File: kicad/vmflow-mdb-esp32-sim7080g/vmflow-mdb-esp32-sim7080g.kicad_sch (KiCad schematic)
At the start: 56 parts, among them J1 MDB_Connector, J2 USB_C_Receptacle_USB2.0_16P, J3 Conn_02x11_Odd_Even, J4 JAE_SIM_Card_SF72S006, J5 Conn_Coaxial, J6 Conn_Coaxial, SW1 SW_Push, U1 TLP785, U2 SIM7080G, U3 ESP32-S3FH4R2, U4 TLP785, U5 LM2594HVM-3.3, Y1 Crystal_GND24

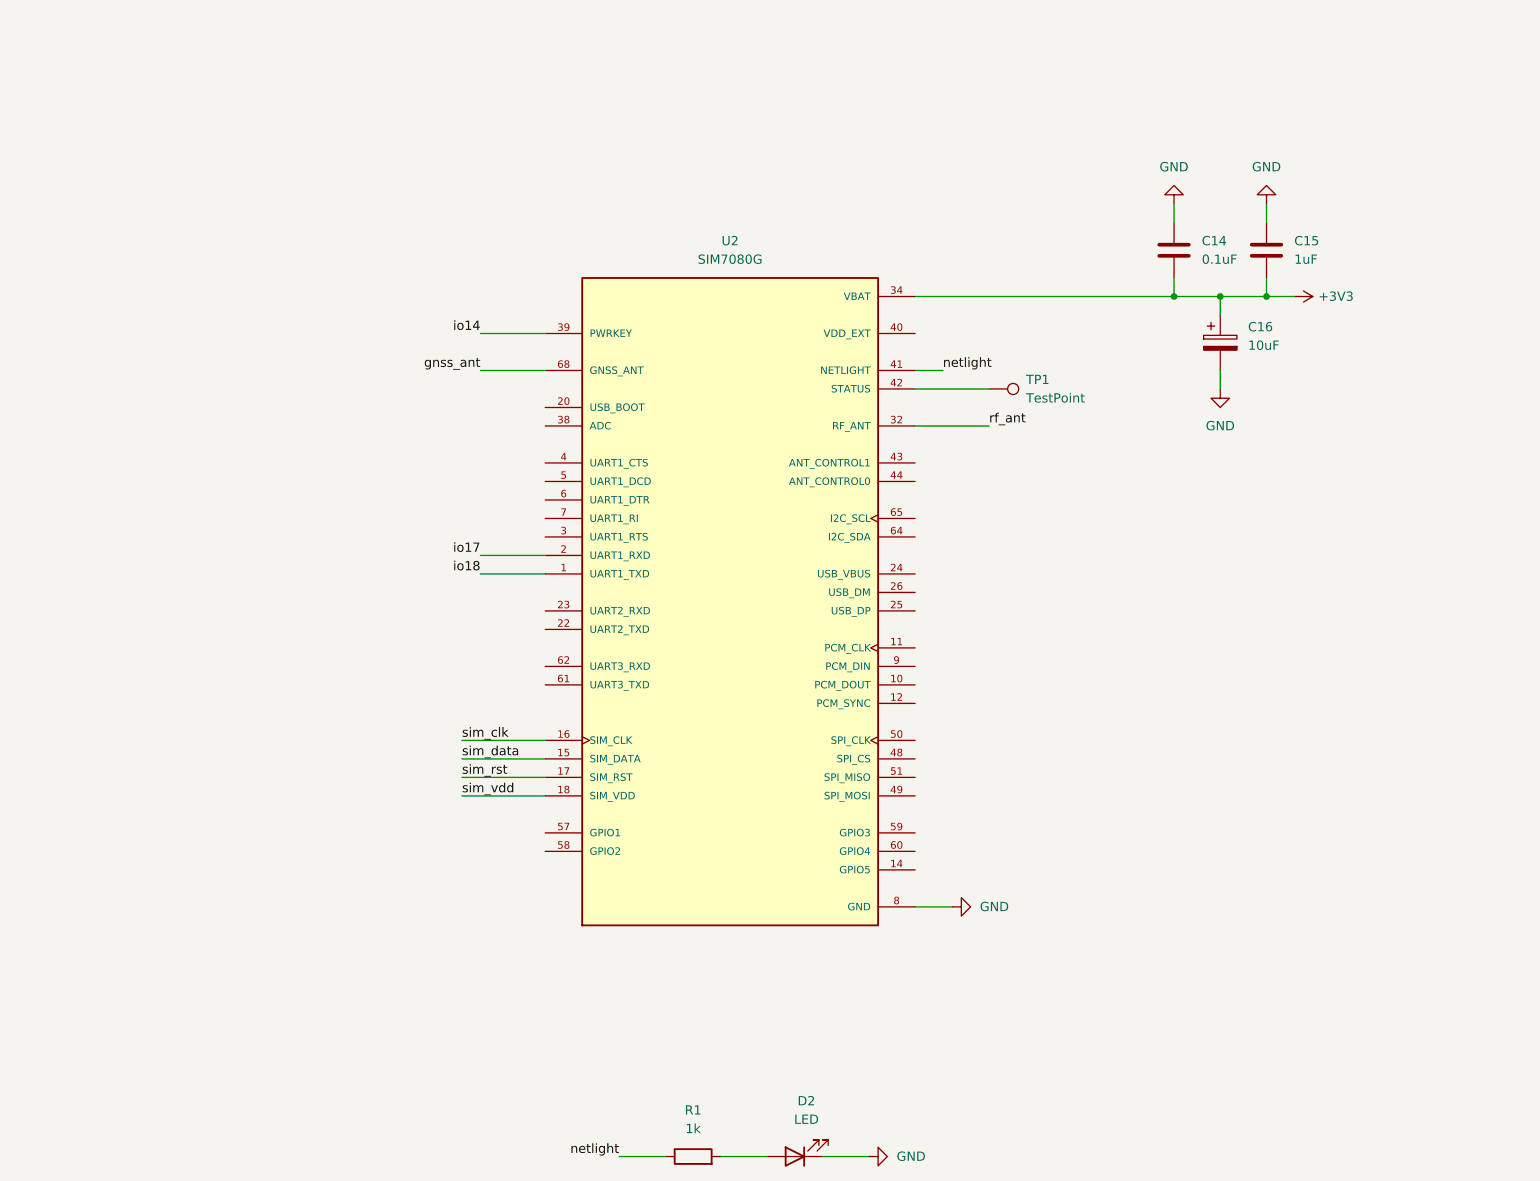
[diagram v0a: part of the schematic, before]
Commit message: Implementing transistor control
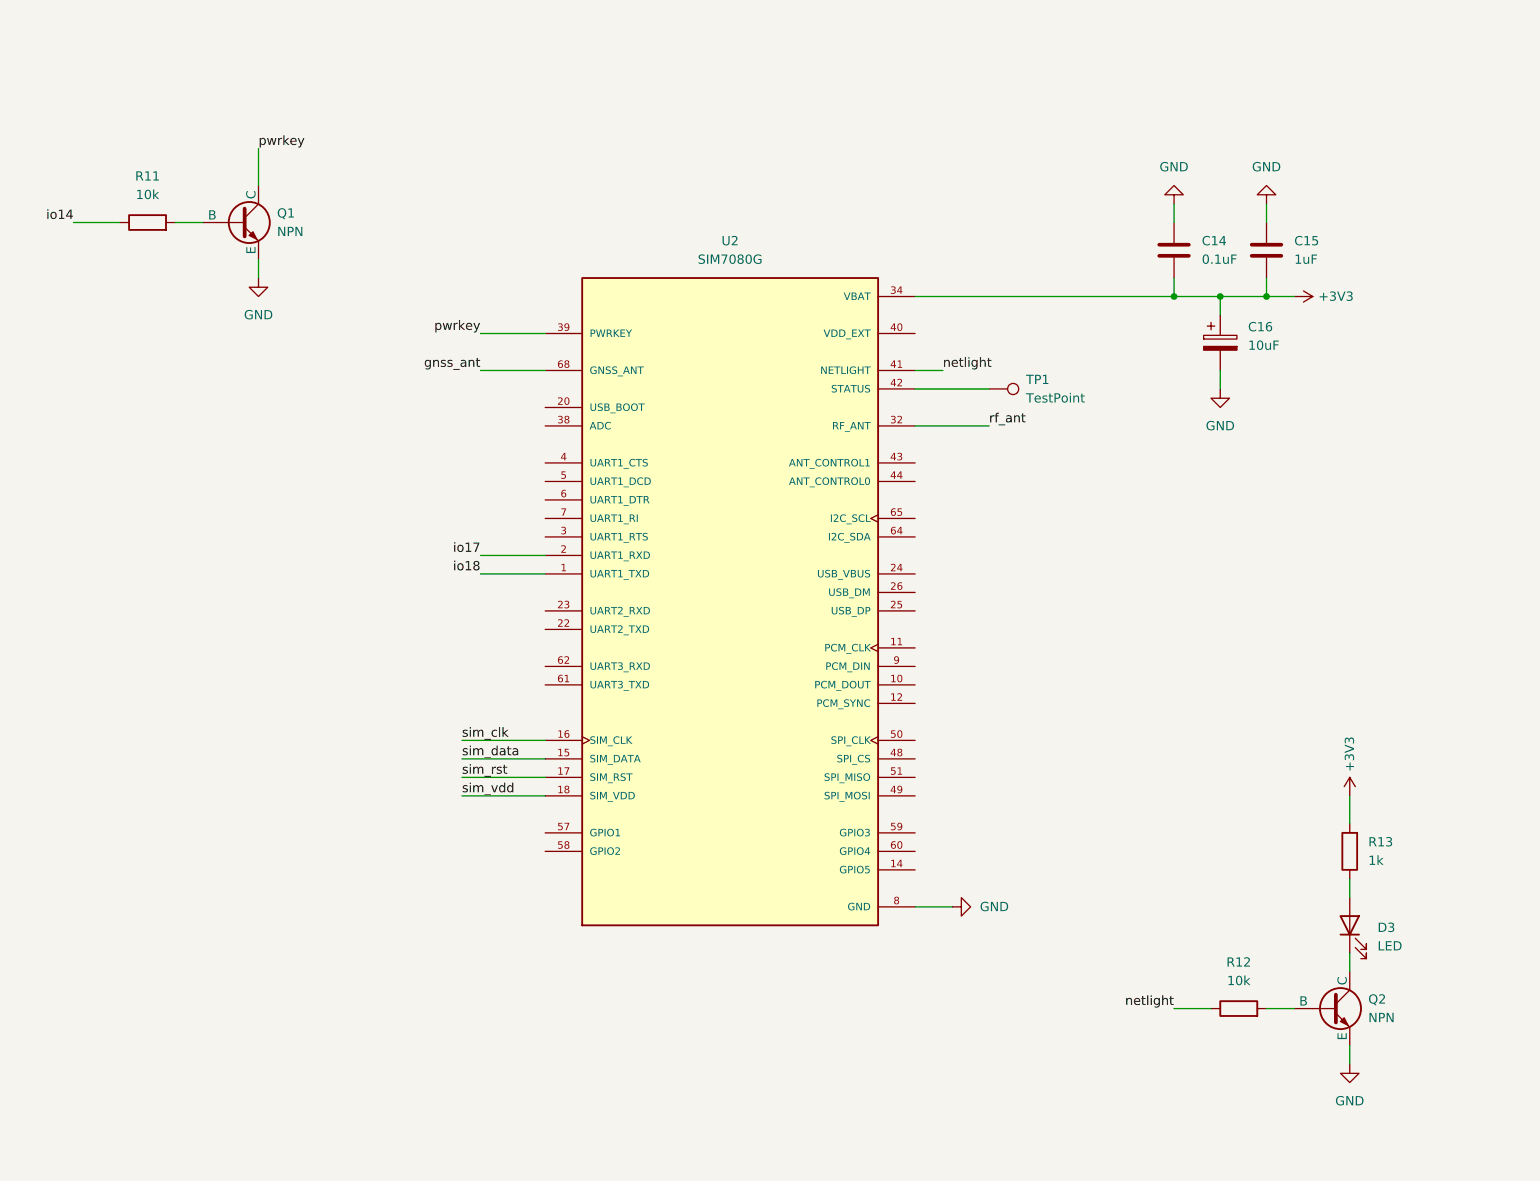
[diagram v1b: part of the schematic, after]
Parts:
- removed D2: LED, LED_SMD:LED_0603_1608Metric, symbol Device:LED
- removed R1: 1k, Resistor_SMD:R_0603_1608Metric, symbol Device:R
- added D3: LED, LED_SMD:LED_0603_1608Metric, symbol Device:LED
- added Q1, Q2: NPN, symbol Simulation_SPICE:NPN
- added R11, R12: 10k, Resistor_SMD:R_0603_1608Metric, symbol Device:R
- added R13: 1k, Resistor_SMD:R_0603_1608Metric, symbol Device:R
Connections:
- net +3V3: now also R13.2
- net GND: now also Q1.3 (E), Q2.3 (E)
- net io14: now also R11.1; no longer U2.39 (PWRKEY)
- net netlight: now also R12.1
- new net: Q2.2 (B), R12.2
- new net: D3.1 (K), Q2.1 (C)
- new net: Q1.2 (B), R11.2
- new net: D3.2 (A), R13.1
- new net pwrkey: Q1.1 (C), U2.39 (PWRKEY)

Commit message: L-shunt -> C-shunt
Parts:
- removed AE1: Antenna, RF_Antenna:Texas_SWRA117D_2.4GHz_Left, symbol Device:Antenna
- removed C4: 1.8pf, Capacitor_SMD:C_0603_1608Metric, symbol Device:C
- removed J6: Conn_Coaxial, Connector_Coaxial:U.FL_Hirose_U.FL-R-SMT-1_Vertical, symbol Connector:Conn_Coaxial
- removed L1: 2.4nh, Inductor_SMD:L_0603_1608Metric, symbol Device:L
- added AE3: Antenna, RF_Antenna:Texas_SWRA117D_2.4GHz_Left, symbol Device:Antenna
- added C21: NC, Capacitor_SMD:C_0603_1608Metric, symbol Device:C
- added C22: 1.8pf, Capacitor_SMD:C_0603_1608Metric, symbol Device:C
- added J7: Conn_Coaxial, Connector_Coaxial:U.FL_Hirose_U.FL-R-SMT-1_Vertical, symbol Connector:Conn_Coaxial
- added L5: 2.4nh, Inductor_SMD:L_0603_1608Metric, symbol Device:L
- J5: LCSC# (none) -> C88374
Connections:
- net GND: now also C21.1, C22.1, J7.2 (Ext)
- net at AE2.1 (A), C18.2, L3.1: now also J7.1 (In)
- net at U3.1 (LNA_IN/RF): now also C21.2, L5.2
- new net: AE3.1 (A), C22.2, L5.1

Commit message: Implementing Level shifter
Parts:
- removed AE2: Antenna, RF_Antenna:Johanson_2450AT43F0100, symbol Device:Antenna
- added Q3: NPN, symbol Simulation_SPICE:NPN
- added R1: 1k2, Resistor_SMD:R_0603_1608Metric, symbol Device:R
- added R14: 1k5, Resistor_SMD:R_0603_1608Metric, symbol Device:R
- added R15: 10k, Resistor_SMD:R_0603_1608Metric, symbol Device:R
- added R16: 1k, Resistor_SMD:R_0603_1608Metric, symbol Device:R
- added R17, R18, R19: 22ohm, Resistor_SMD:R_0603_1608Metric, symbol Device:R
- C17: value 1.8pf -> NC; LCSC# C376773 -> (none)
- C18: value 1.8pf -> 27pf; LCSC# C376773 -> (none)
- C19: value 1.8pf -> 27pf
- C20: value 1.8pf -> NC
- L3: value 2.4nh -> 47nh; LCSC# C2042508 -> (none)
- L4: value 2.4nh -> 47nh
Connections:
- net +3V3: now also R16.1
- net GND: now also Q3.3 (E), R14.2
- net io17: now also R1.1; no longer U2.2 (UART1_RXD)
- net io18: now also Q3.1 (C), R16.2; no longer U2.1 (UART1_TXD)
- net sim_clk: now also R17.1; no longer J4.C3 (CLK)
- net sim_data: now also R18.1; no longer J4.C7 (I/O)
- net sim_rst: now also R19.1; no longer J4.C2 (RST)
- new net: Q3.2 (B), R15.1
- new net: J4.C2 (RST), R19.2
- new net: J4.C3 (CLK), R17.2
- new net: J4.C7 (I/O), R18.2
- new net sim_uart1_rx: R1.2, R14.1, U2.2 (UART1_RXD)
- new net sim_uart1_tx: R15.2, U2.1 (UART1_TXD)
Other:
- moved on the sheet: C17, C18, C19, C20, J5, J7, L3, L4

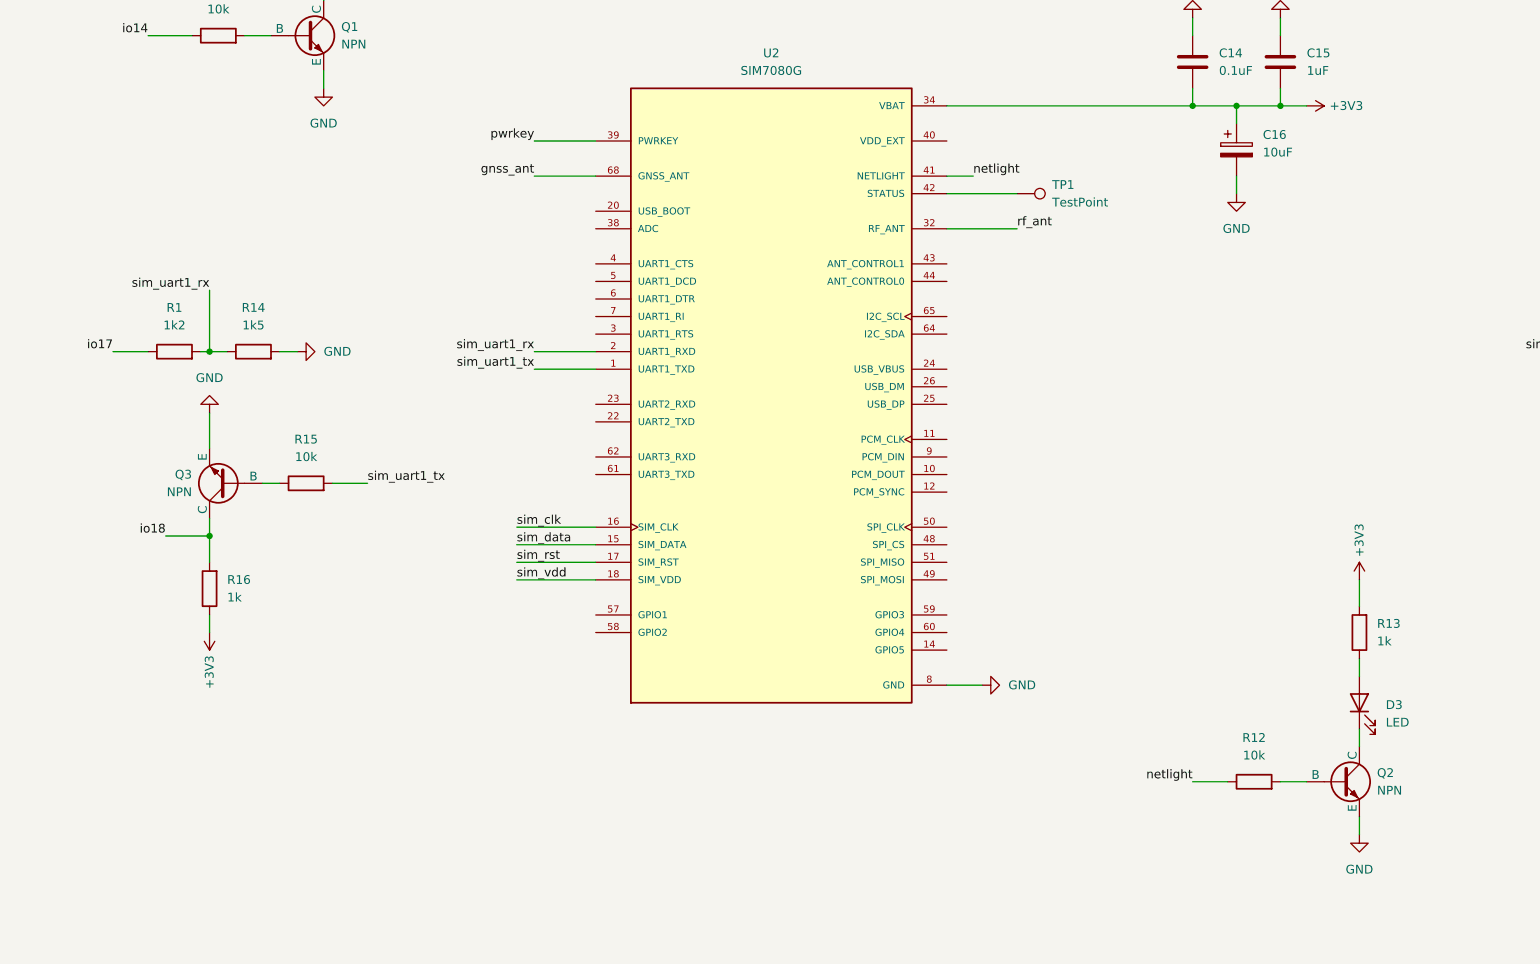
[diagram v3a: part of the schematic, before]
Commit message: Implementing transistor sift level
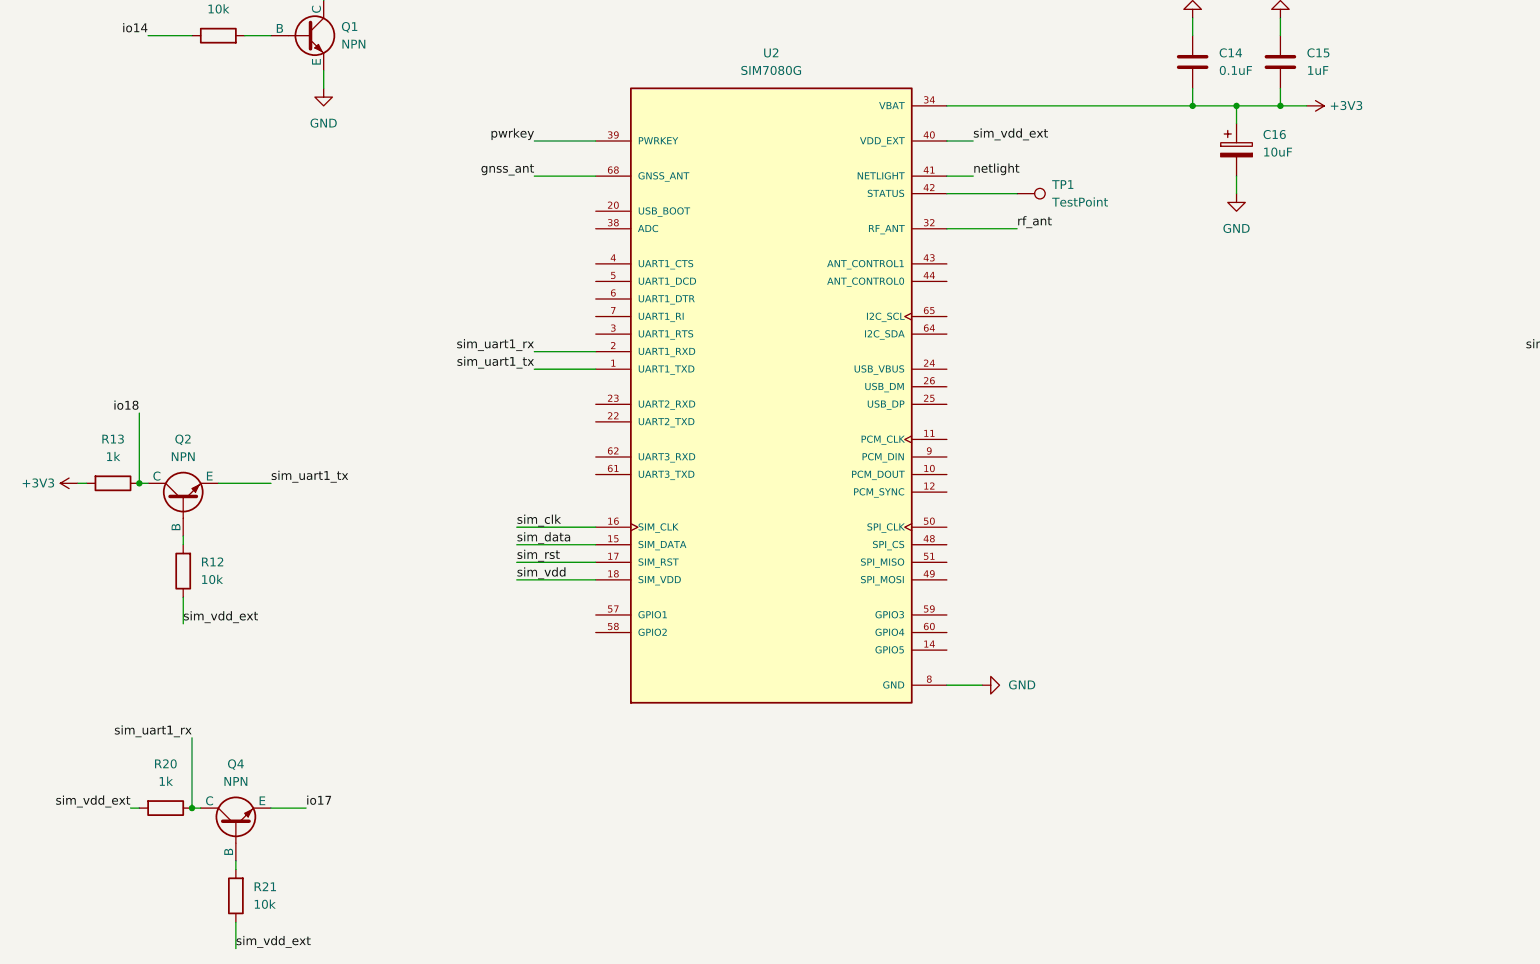
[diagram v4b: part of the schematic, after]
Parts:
- removed D3: LED, LED_SMD:LED_0603_1608Metric, symbol Device:LED
- removed Q3: NPN, symbol Simulation_SPICE:NPN
- removed R1: 1k2, Resistor_SMD:R_0603_1608Metric, symbol Device:R
- removed R14: 1k5, Resistor_SMD:R_0603_1608Metric, symbol Device:R
- removed R15: 10k, Resistor_SMD:R_0603_1608Metric, symbol Device:R
- removed R16: 1k, Resistor_SMD:R_0603_1608Metric, symbol Device:R
- added Q4: NPN, symbol Simulation_SPICE:NPN
- added R20: 1k, Resistor_SMD:R_0603_1608Metric, symbol Device:R
- added R21: 10k, Resistor_SMD:R_0603_1608Metric, symbol Device:R
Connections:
- net GND: no longer Q2.3 (E)
- net io17: now also Q4.3 (E)
- net io18: now also Q2.1 (C), R13.1
- net netlight: no longer R12.1
- net sim_uart1_rx: now also Q4.1 (C), R20.1
- net sim_uart1_tx: now also Q2.3 (E)
- net sim_vdd_ext: now reaches U2.40 (VDD_EXT)
- net sim_vdd_ext: now also R12.1, R20.2, R21.1
- new net: Q4.2 (B), R21.2

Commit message: Setting LCSC# components
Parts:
- removed R13: 1k, Resistor_SMD:R_0603_1608Metric, symbol Device:R
- added R1: 4K7, Resistor_SMD:R_0603_1608Metric, symbol Device:R
- C16: LCSC# C30242 -> C110053
- Q1, Q2, Q4: LCSC# (none) -> C916374
- R11, R21: value 10k -> 4K7; LCSC# C98220 -> C23162
- R12: value 10k -> 10K
- R17, R18, R19: LCSC# C98220 -> C23345
- R20: value 1k -> 10K; LCSC# C2907113 -> C98220
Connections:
- net +3V3: now also R12.2
- net io14: now also R1.2; no longer R11.1
- net io18: now also R12.1
- net sim_vdd_ext: now also R11.1; no longer R12.1
- net at Q1.2 (B): now also R1.1; no longer R11.2
- net at Q2.2 (B): now also R11.2; no longer R12.2

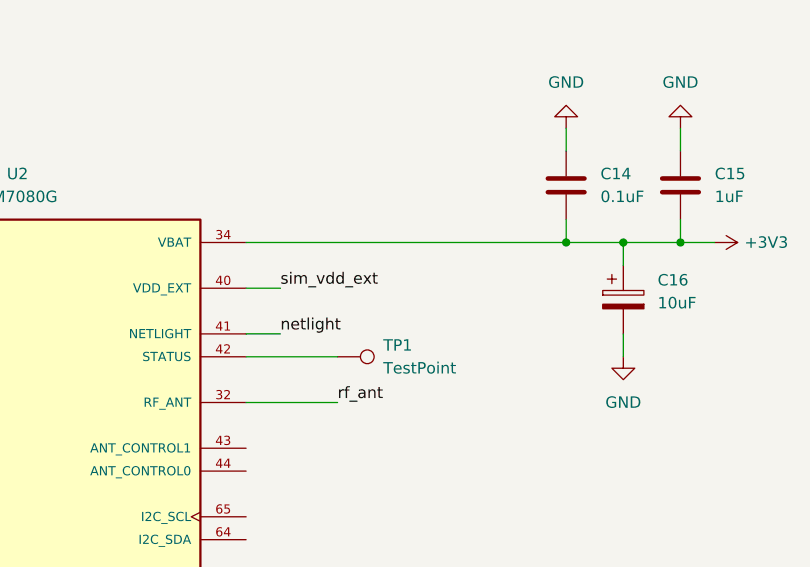
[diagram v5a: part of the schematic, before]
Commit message: vdd_ext <- test_point
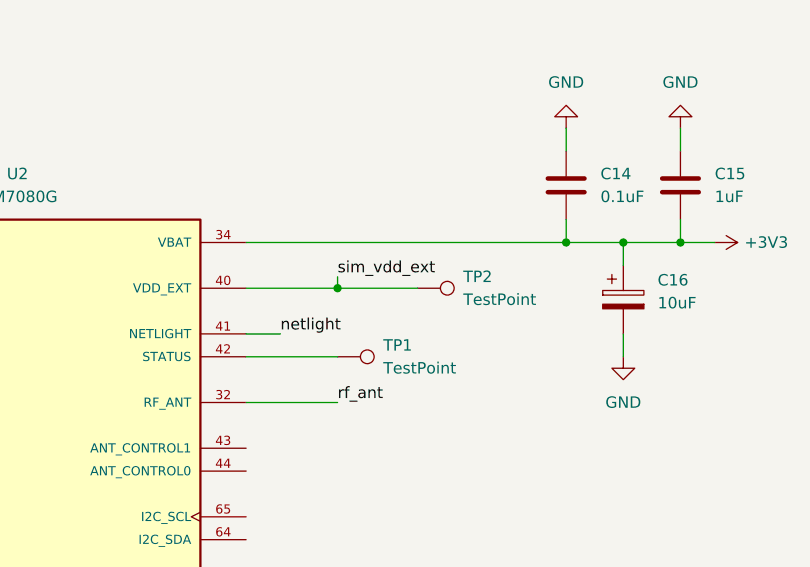
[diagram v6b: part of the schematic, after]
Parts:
- added TP2: TestPoint, TestPoint:TestPoint_Pad_D1.0mm, symbol Connector:TestPoint
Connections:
- net sim_vdd_ext: now also TP2.1
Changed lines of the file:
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@@
 	)
 	(junction
+		(at 163.83 276.86)
+		(diameter 0)
+		(color 0 0 0 0)
+	)
+	(junction
 		(at 81.28 133.35)
 		(diameter 0)
@@
 	(wire
 		(pts
+			(xy 163.83 276.86) (xy 153.67 276.86)
+		)
+		(stroke
+			(width 0)
+			(type default)
+		)
+	)
+	(wire
+		(pts
 			(xy 63.5 123.19) (xy 86.36 123.19)
 		)
@@
 	(wire
 		(pts
+			(xy 163.83 276.86) (xy 172.72 276.86)
+		)
+		(stroke
+			(width 0)
+			(type default)
+		)
+	)
+	(wire
+		(pts
 			(xy 386.08 149.86) (xy 386.08 147.32)
 		)
@@
 	(wire
 		(pts
-			(xy 157.48 276.86) (xy 153.67 276.86)
-		)
-		(stroke
-			(width 0)
-			(type default)
-		)
-	)
-	(wire
-		(pts
 			(xy 165.1 115.57) (xy 167.64 115.57)
 		)
@@
 	(wire
 		(pts
+			(xy 163.83 275.59) (xy 163.83 276.86)
+		)
+		(stroke
+			(width 0)
+			(type default)
+		)
+	)
+	(wire
+		(pts
 			(xy 269.24 132.08) (xy 284.48 132.08)
 		)
@@
 	)
 	(label "sim_vdd_ext"
-		(at 157.48 276.86 0)
+		(at 163.83 275.59 0)
 		(effects
 			(font
@@
 					(unit 1)
 				)
+			)
+		)
+	)
+	(symbol
+		(lib_id "Connector:TestPoint")
+		(at 172.72 276.86 270)
+		(unit 1)
+		(exclude_from_sim no)
+		(in_bom yes)
+		(on_board yes)
+		(dnp no)
+		(fields_autoplaced yes)
+		(property "Reference" "TP2"
+			(at 177.8 275.5899 90)
+			(effects
+				(font
+					(size 1.27 1.27)
+				)
+				(justify left)
+			)
+		)
+		(property "Value" "TestPoint"
+			(at 177.8 278.1299 90)
+			(effects
+				(font
+					(size 1.27 1.27)
+				)
+				(justify left)
+			)
+		)
+		(property "Footprint" "TestPoint:TestPoint_Pad_D1.0mm"
+			(at 172.72 281.94 0)
+			(effects
+				(font
+					(size 1.27 1.27)
+				)
+				(hide yes)
+			)
+		)
+		(property "Datasheet" "~"
+			(at 172.72 281.94 0)
+			(effects
+				(font
+					(size 1.27 1.27)
+				)
+				(hide yes)
+			)
+		)
+		(property "Description" "test point"
+			(at 172.72 276.86 0)
+			(effects
+				(font
+					(size 1.27 1.27)
+				)
+				(hide yes)
+			)
+		)
+		(pin "1"
+		)
+		(instances
+			(project "vmflow-mdb-esp32-sim7080g"
+				(path "/95980b25-0707-441d-ba83-7f6c6e1d1aaa"
+					(reference "TP2")
+					(unit 1)
+				)

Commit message: LCSC# references
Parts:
- U2: LCSC# (none) -> C2943992
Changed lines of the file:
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@@
+			)
+		)
+		(property "LCSC#" "C2943992"
+			(at 128.27 312.42 0)
+			(effects
+				(font
+					(size 1.27 1.27)
+				)
+				(hide yes)
 			)
 		)
